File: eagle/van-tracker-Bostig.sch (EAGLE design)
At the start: 15 parts, among them K1 CP1-12V, Q1 TIP122, X1 EZG-2K-302, X2 EZG-2K-302

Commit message: 2.failed attempt to use the connection that the kill switch is breaking AS the SIGNAL to break the connection (yeah it didn't work)
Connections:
- removed net N$17: 12V-5V_CONVERTER.+VIN1, D1.C, K11.2, SWITCHG$2.1
- removed net N$8: K12.O
- new net N$20: 12V-5V_CONVERTER.+VIN1, SWITCHG$2.1
- new net N$21: K12.O, Q1.E
- net N$2: no longer Q1.E
- net N$7: now also D1.C, K11.2
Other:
- note added: "This does NOT WORK. The relay never opens because the current flows through the relay switch, which is normally closed"
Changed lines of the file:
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@@
 <text x="-41.402" y="32.004" size="1.778" layer="91">Starting line in (20A max)</text>
 <text x="-41.402" y="22.098" size="1.778" layer="91">Starting line out (20A max)</text>
+<text x="-63.5" y="43.18" size="1.778" layer="91">This does NOT WORK.
+The relay never opens because the current
+flows through the relay switch, which is
+normally closed </text>
 </plain>
 <instances>
@@
 <segment>
 <pinref part="12V-5V_CONVERTER" gate="G$1" pin="-VIN1"/>
-<wire x1="-10.16" y1="60.96" x2="-10.16" y2="-17.78" width="0.1524" layer="91"/>
-<wire x1="-10.16" y1="-17.78" x2="20.32" y2="-17.78" width="0.1524" layer="91"/>
-<pinref part="Q1" gate="G$1" pin="E"/>
-<wire x1="20.32" y1="-17.78" x2="20.32" y2="-15.24" width="0.1524" layer="91"/>
 <pinref part="X1" gate="G$1" pin="2"/>
 <wire x1="-17.78" y1="80.264" x2="-30.48" y2="80.264" width="0.1524" layer="91"/>
 <wire x1="-30.48" y1="80.264" x2="-30.48" y2="60.96" width="0.1524" layer="91"/>
 <wire x1="-30.48" y1="60.96" x2="-10.16" y2="60.96" width="0.1524" layer="91"/>
-<junction x="-10.16" y="60.96"/>
 </segment>
 </net>
@@
 <pinref part="K1" gate="2" pin="P"/>
 <wire x1="7.62" y1="27.94" x2="7.62" y2="30.48" width="0.1524" layer="91"/>
-<wire x1="7.62" y1="30.48" x2="-33.02" y2="30.48" width="0.1524" layer="91"/>
+<wire x1="7.62" y1="30.48" x2="-10.16" y2="30.48" width="0.1524" layer="91"/>
 <junction x="-33.02" y="30.48"/>
-</segment>
-</net>
-<net name="N$8" class="0">
-<segment>
-<junction x="-33.02" y="20.32"/>
-<pinref part="K1" gate="2" pin="O"/>
-<wire x1="2.54" y1="20.32" x2="-33.02" y2="20.32" width="0.1524" layer="91"/>
+<wire x1="-10.16" y1="30.48" x2="-33.02" y2="30.48" width="0.1524" layer="91"/>
+<wire x1="-10.16" y1="30.48" x2="-10.16" y2="48.26" width="0.1524" layer="91"/>
+<junction x="-10.16" y="30.48"/>
+<wire x1="-10.16" y1="48.26" x2="20.32" y2="48.26" width="0.1524" layer="91"/>
+<pinref part="K1" gate="1" pin="2"/>
+<wire x1="20.32" y1="40.64" x2="20.32" y2="27.94" width="0.1524" layer="91"/>
+<pinref part="D1" gate="1" pin="C"/>
+<wire x1="33.02" y1="25.4" x2="33.02" y2="40.64" width="0.1524" layer="91"/>
+<wire x1="33.02" y1="40.64" x2="20.32" y2="40.64" width="0.1524" layer="91"/>
+<wire x1="20.32" y1="48.26" x2="20.32" y2="40.64" width="0.1524" layer="91"/>
+<junction x="20.32" y="40.64"/>
 </segment>
 </net>
@@
 </segment>
 </net>
-<net name="N$17" class="0">
-<segment>
-<pinref part="12V-5V_CONVERTER" gate="G$1" pin="+VIN1"/>
-<pinref part="SWITCH" gate="G$2" pin="1"/>
-<wire x1="-10.16" y1="66.04" x2="-12.7" y2="66.04" width="0.1524" layer="91"/>
-<wire x1="-12.7" y1="66.04" x2="-15.24" y2="66.04" width="0.1524" layer="91"/>
-<wire x1="-12.7" y1="66.04" x2="-12.7" y2="50.8" width="0.1524" layer="91"/>
-<junction x="-12.7" y="66.04"/>
-<wire x1="-12.7" y1="50.8" x2="20.32" y2="50.8" width="0.1524" layer="91"/>
-<pinref part="K1" gate="1" pin="2"/>
-<wire x1="20.32" y1="40.64" x2="20.32" y2="27.94" width="0.1524" layer="91"/>
-<pinref part="D1" gate="1" pin="C"/>
-<wire x1="33.02" y1="25.4" x2="33.02" y2="40.64" width="0.1524" layer="91"/>
-<wire x1="33.02" y1="40.64" x2="20.32" y2="40.64" width="0.1524" layer="91"/>
-<wire x1="20.32" y1="50.8" x2="20.32" y2="40.64" width="0.1524" layer="91"/>
-<junction x="20.32" y="40.64"/>
-</segment>
-</net>
 <net name="N$5" class="0">
 <segment>
@@
 </segment>
 </net>
+<net name="N$20" class="0">
+<segment>
+<pinref part="SWITCH" gate="G$2" pin="1"/>
+<pinref part="12V-5V_CONVERTER" gate="G$1" pin="+VIN1"/>
+<wire x1="-10.16" y1="66.04" x2="-15.24" y2="66.04" width="0.1524" layer="91"/>
+</segment>
+</net>
+<net name="N$21" class="0">
+<segment>
+<pinref part="Q1" gate="G$1" pin="E"/>
+<wire x1="-10.16" y1="-17.78" x2="20.32" y2="-17.78" width="0.1524" layer="91"/>
+<wire x1="20.32" y1="-17.78" x2="20.32" y2="-15.24" width="0.1524" layer="91"/>
+<junction x="-33.02" y="20.32"/>
+<pinref part="K1" gate="2" pin="O"/>
+<wire x1="2.54" y1="20.32" x2="-10.16" y2="20.32" width="0.1524" layer="91"/>
+<wire x1="-10.16" y1="20.32" x2="-33.02" y2="20.32" width="0.1524" layer="91"/>
+<wire x1="-10.16" y1="-17.78" x2="-10.16" y2="20.32" width="0.1524" layer="91"/>
+<junction x="-10.16" y="20.32"/>
+</segment>
+</net>
 </nets>
 </sheet>
@@
 </drawing>
 <compatibility>
+<note version="6.3" minversion="6.2.2" severity="warning">
+Since Version 6.2.2 text objects can contain more than one line,
+which will not be processed correctly with this version.
+</note>
 <note version="8.2" severity="warning">
 Since Version 8.2, EAGLE supports online libraries. The ids

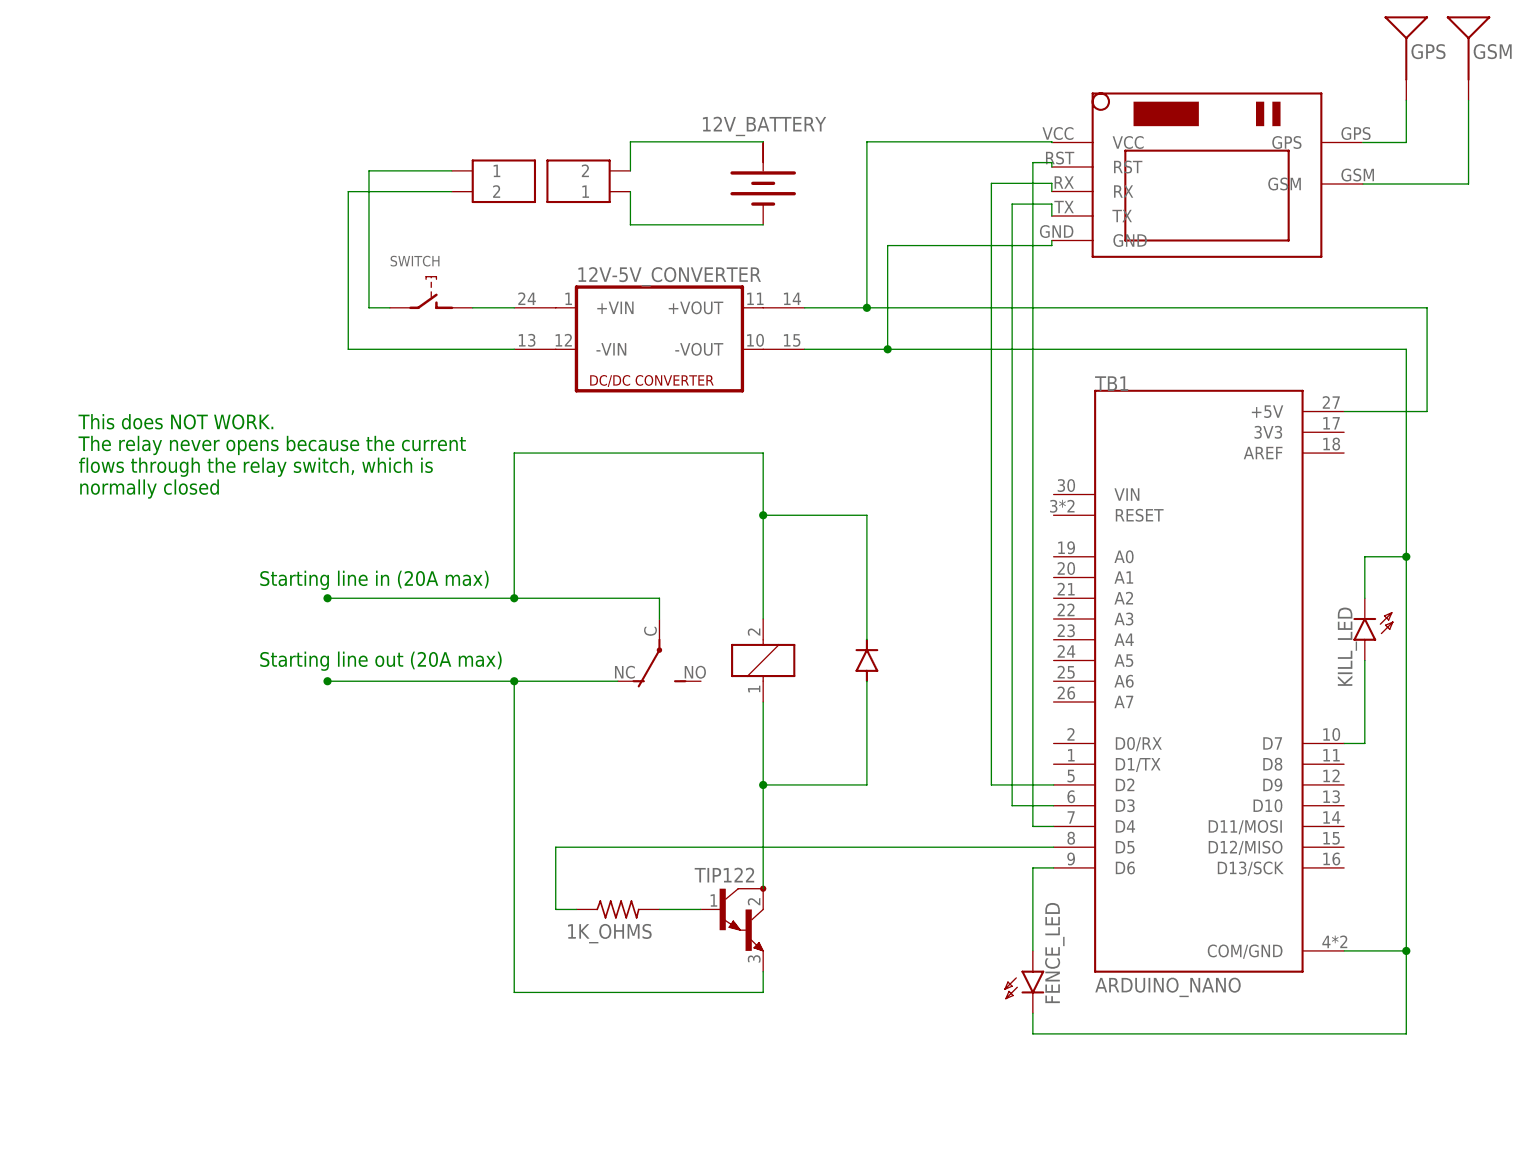
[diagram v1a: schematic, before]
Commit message: 3.to get kill switch signal use interrupt
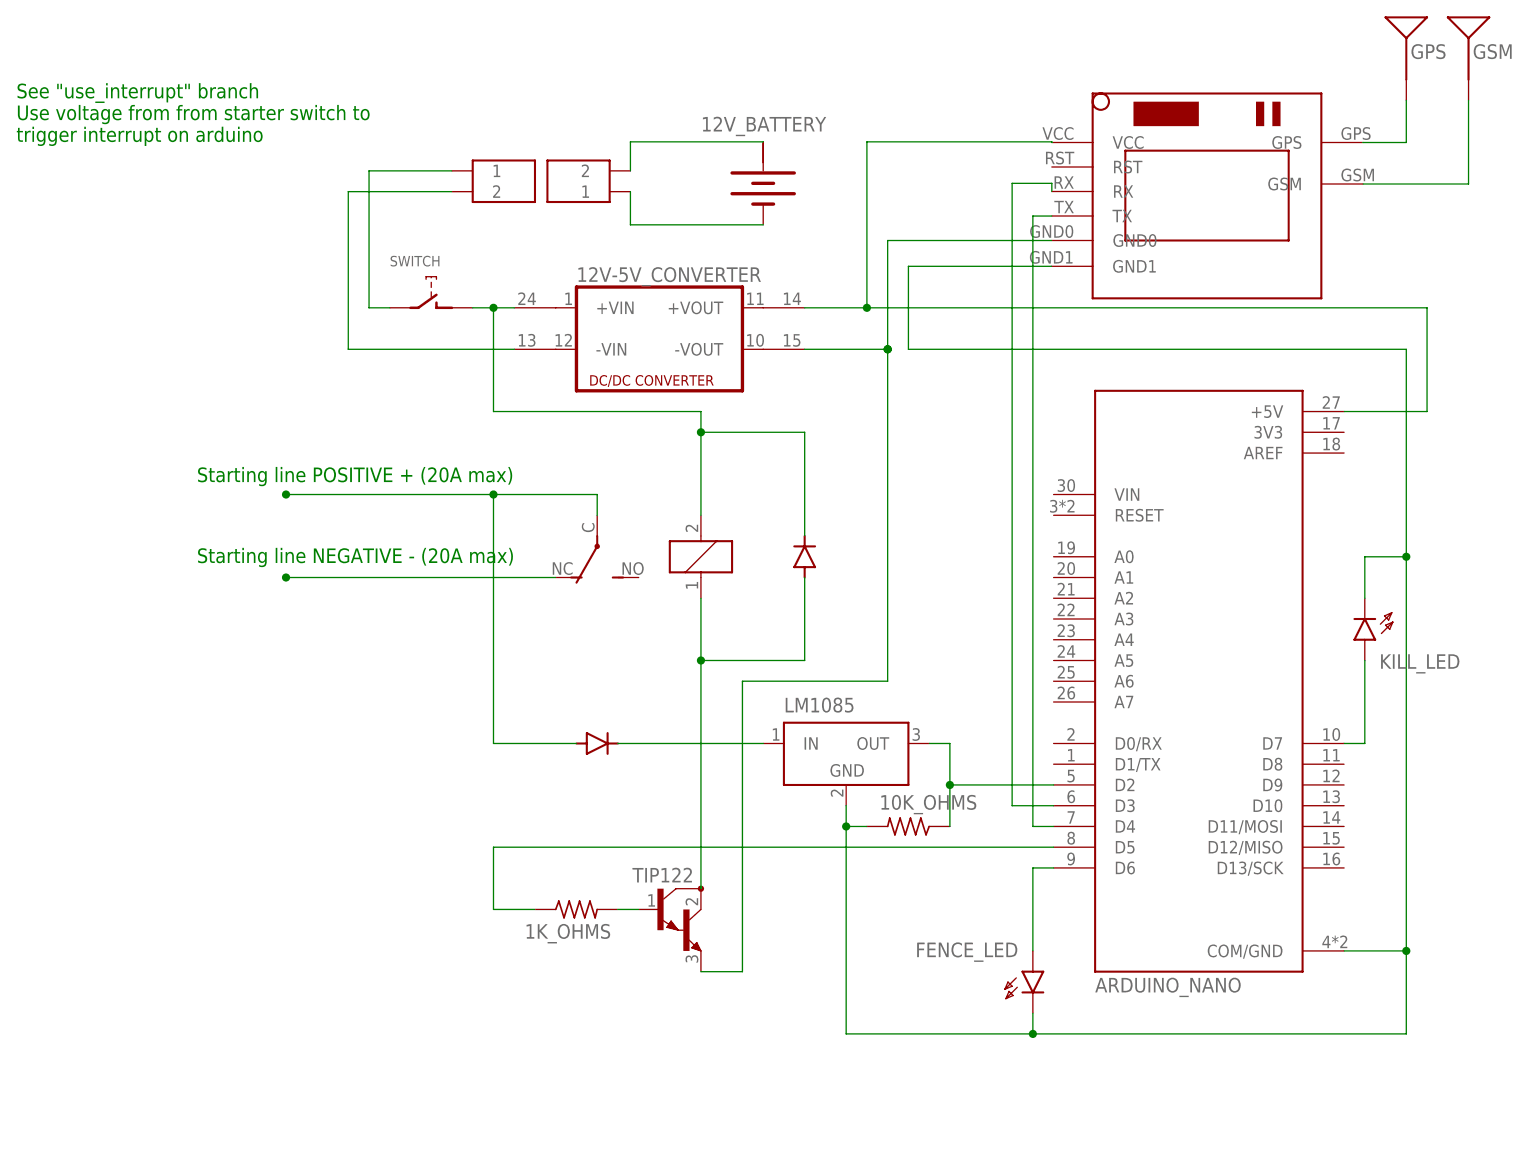
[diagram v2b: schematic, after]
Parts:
- added 10K_OHMS: (no value), rcl:R-US_0411/15
- added D2: 1N5400, diode:1N5400
- added LM1085: LT1963EST-2.5, linear-technology:LT1963EST-2.5
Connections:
- new net N$17: 12V-5V_CONVERTER.+VIN1, D1.C, K11.2, SWITCHG$2.1
- new net N$8: K12.O
- net N$10: now also 10K_OHMS.2, LM1085G$1.GND, U$1.GND1; no longer 12V-5V_CONVERTER.-VOUT1, U$1.GND
- net N$11: now also TB1.D3; no longer TB1.D2
- net N$12: now also TB1.D4; no longer TB1.D3
- net N$13: now also 12V-5V_CONVERTER.-VOUT1, Q1.E, U$1.GND0; no longer TB1.D4, U$1.RST
- net N$20: now also 10K_OHMS.1, LM1085G$1.OUT, TB1.D2; no longer 12V-5V_CONVERTER.+VIN1, SWITCHG$2.1
- net N$21: now also D2.C, LM1085G$1.IN; no longer K12.O, Q1.E
- net N$7: now also D2.A; no longer D1.C, K11.2
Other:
- note added: "See "use_interrupt" branch Use voltage from from starter switch to trigger interrupt on arduino"
- note added: "Starting line NEGATIVE - (20A max)"
- note added: "Starting line POSITIVE + (20A max)"
- note removed: "Starting line in (20A max)"
- note removed: "Starting line out (20A max)"
- note removed: "This does NOT WORK. The relay never opens because the current flows through the relay switch, which is normally closed"
- moved on the sheet: 1K_OHMS

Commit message: 1.to get kill switch signal use a second transistor (safer and simpler than interrupt)
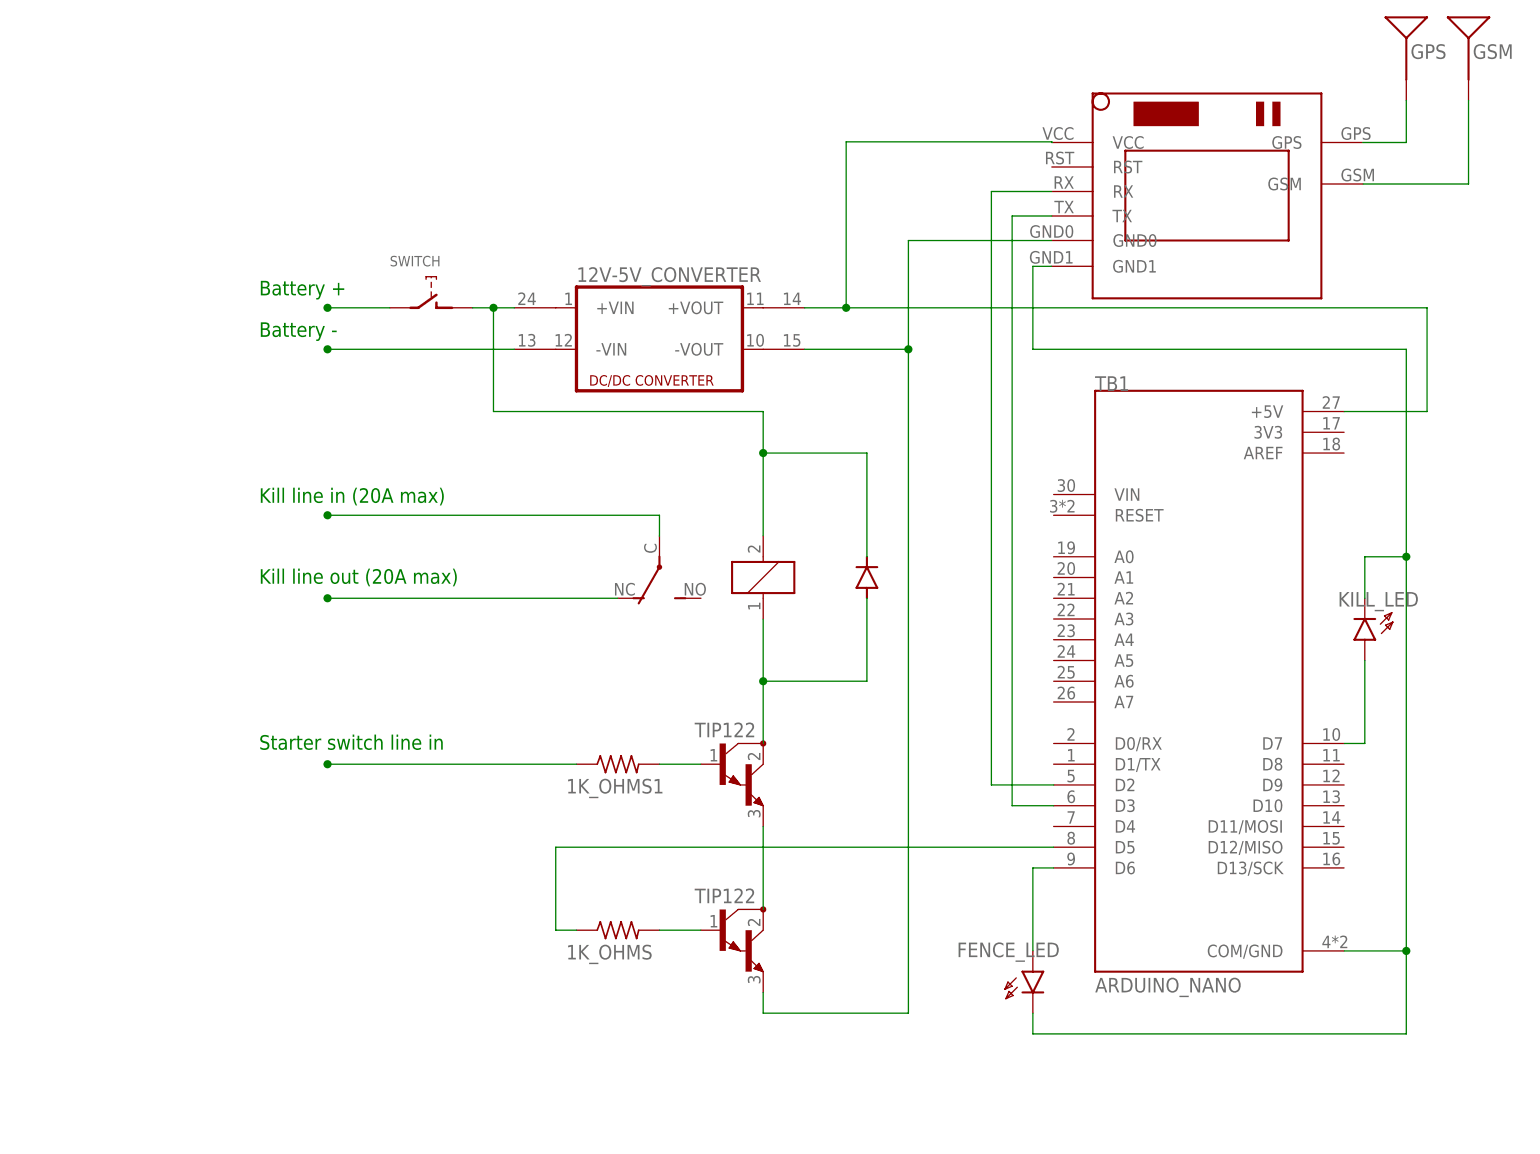
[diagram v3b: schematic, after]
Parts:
- removed 10K_OHMS: (no value), rcl:R-US_0411/15
- removed 12V_BATTERY: (no value), special:BATTERY
- removed D2: 1N5400, diode:1N5400
- removed LM1085: LT1963EST-2.5, linear-technology:LT1963EST-2.5
- removed X1, X2: EZG-2K-302, con-lemo:EZG-2K-302
- added 1K_OHMS1: (no value), rcl:R-US_0411/15
- added Q2: TIP122, transistor-npn:TIP122
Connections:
- removed net N$10: 10K_OHMS.2, FENCE_LED.K, KILL_LED.K, LM1085G$1.GND, TB1.COM/GND, U$1.GND1
- removed net N$18: 12V_BATTERY.-, X2.1
- removed net N$19: SWITCHG$2.2, X1.1
- new net N$13: 1K_OHMS1.2, Q2.B
- new net N$22: FENCE_LED.K, KILL_LED.K, TB1.COM/GND, U$1.GND1
- net N$1: now also SWITCHG$2.2; no longer 12V_BATTERY.+, X2.2
- net N$11: now also TB1.D2; no longer TB1.D3
- net N$12: now also TB1.D3; no longer TB1.D4
- net N$2: no longer X1.2
- net N$20: now also Q1.C, Q2.E; no longer 10K_OHMS.1, LM1085G$1.OUT, TB1.D2
- net N$21: now also 1K_OHMS1.1; no longer D2.C, LM1085G$1.IN
- net N$5: now also Q2.C; no longer Q1.C
- net N$7: no longer D2.A
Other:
- note added: "Battery +"
- note added: "Battery -"
- note added: "Kill line in (20A max)"
- note added: "Kill line out (20A max)"
- note added: "Starter switch line in"
- note removed: "See "use_interrupt" branch Use voltage from from starter switch to trigger interrupt on arduino"
- note removed: "Starting line NEGATIVE - (20A max)"
- note removed: "Starting line POSITIVE + (20A max)"
- moved on the sheet: 1K_OHMS
